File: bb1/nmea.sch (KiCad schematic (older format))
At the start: 30 parts, among them P1 PWR+CAN, P5 NMEA_RX, P7 NMEA_TX, P8 BATTERIES, P9 SHUNT, U10 MCP2562, U11 SN75C3222E, U12 INA219

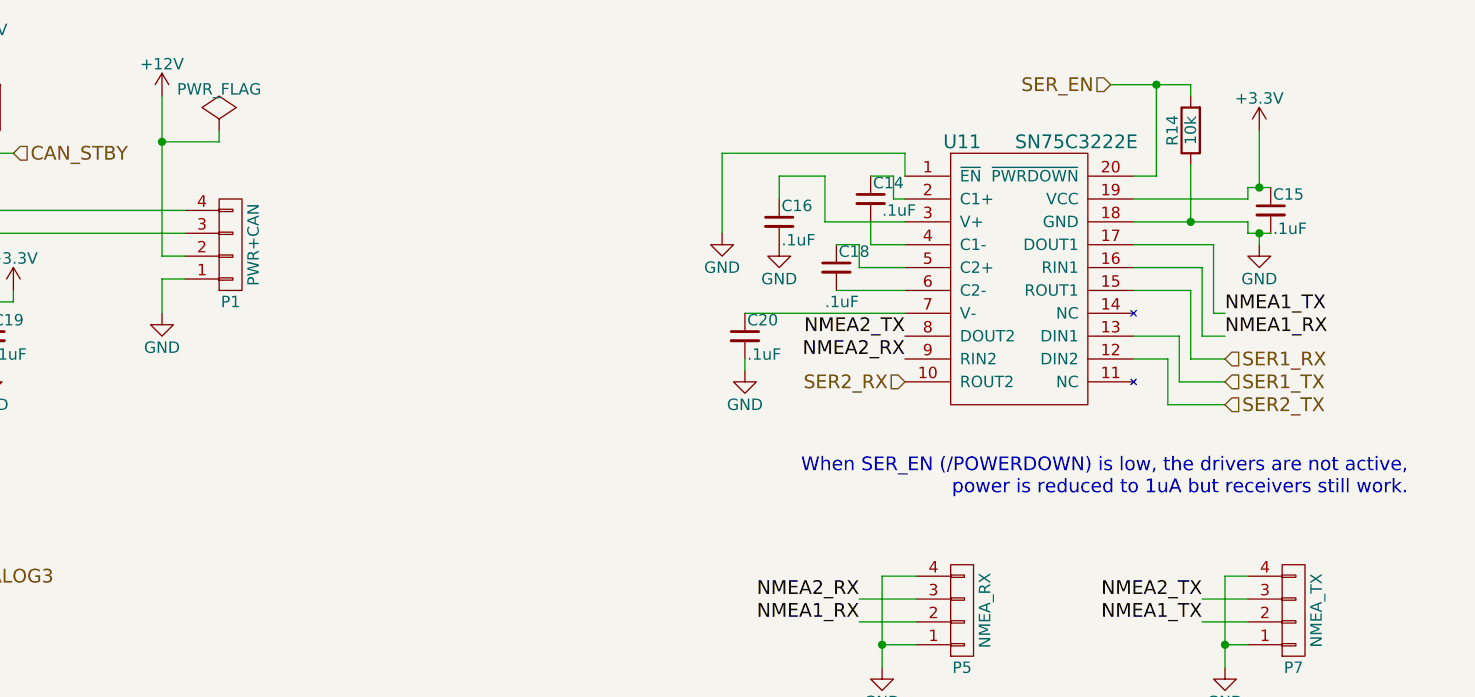
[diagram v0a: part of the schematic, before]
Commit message: Fine tuning of the board
- Added test headers for serial1, serial2 and can (at 3.3v levels)
- Added solder jumpers to disconnect serial2 from rs232 converter
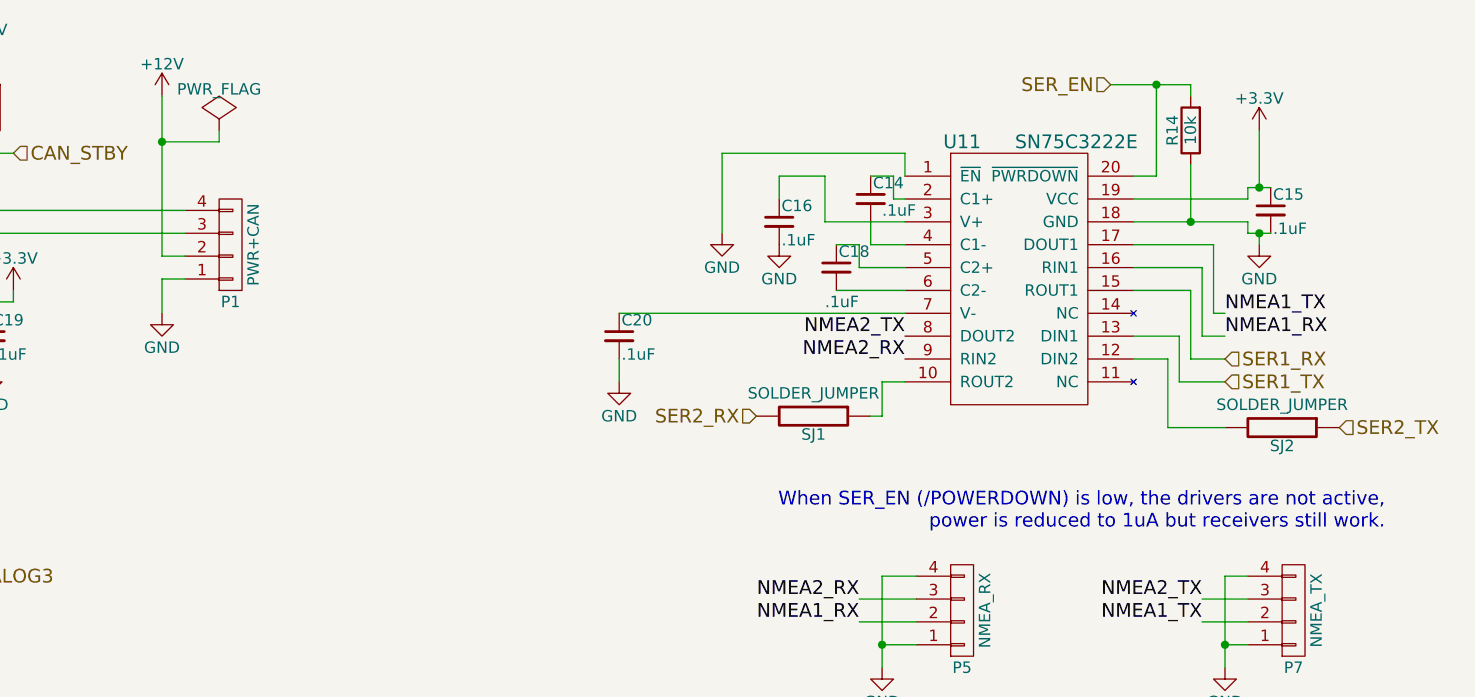
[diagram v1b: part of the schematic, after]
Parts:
- added SJ1, SJ2: SOLDER_JUMPER, bb:SolderJumper, symbol SOLDER_JUMPER
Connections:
- net SER2_RX: now also SJ1.2; no longer U11.10 (ROUT2)
- net SER2_TX: now also SJ2.1; no longer U11.12 (DIN2)
- new net: SJ1.1, U11.10 (ROUT2)
- new net: SJ2.2, U11.12 (DIN2)
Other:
- moved on the sheet: C20
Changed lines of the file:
@@
 L C_Small C20
 U 1 1 56606B8F
-P 6700 2400
-F 0 "C20" H 6710 2470 50  0000 L CNN
-F 1 ".1uF" H 6710 2320 50  0000 L CNN
-F 2 "Capacitors_SMD:C_0603_HandSoldering" H 6700 2400 60  0001 C CNN
-F 3 "" H 6700 2400 60  0000 C CNN
-	1    6700 2400
+P 6150 2400
+F 0 "C20" H 6160 2470 50  0000 L CNN
+F 1 ".1uF" H 6160 2320 50  0000 L CNN
+F 2 "Capacitors_SMD:C_0603_HandSoldering" H 6150 2400 60  0001 C CNN
+F 3 "" H 6150 2400 60  0000 C CNN
+	1    6150 2400
 	1    0    0    -1
 $EndComp
@@
 	7100 2200 7400 2200
 Wire Wire Line
-	7400 2300 6700 2300
-Wire Wire Line
-	6700 2500 6700 2550
+	7400 2300 6150 2300
+Wire Wire Line
+	6150 2500 6150 2600
 $Comp
 L GND #PWR064
 U 1 1 56606BD2
-P 6700 2550
-F 0 "#PWR064" H 6700 2300 50  0001 C CNN
-F 1 "GND" H 6700 2400 50  0000 C CNN
-F 2 "" H 6700 2550 60  0000 C CNN
-F 3 "" H 6700 2550 60  0000 C CNN
-	1    6700 2550
+P 6150 2600
+F 0 "#PWR064" H 6150 2350 50  0001 C CNN
+F 1 "GND" H 6150 2450 50  0000 C CNN
+F 2 "" H 6150 2600 60  0000 C CNN
+F 3 "" H 6150 2600 60  0000 C CNN
+	1    6150 2600
 	1    0    0    -1
 $EndComp
@@
 	8400 2500 8550 2500
 Wire Wire Line
-	8550 2500 8550 2700
-Wire Wire Line
-	8550 2700 8800 2700
+	8550 2500 8550 2800
+Wire Wire Line
+	8550 2800 8800 2800
 Text Label 7400 2400 2    60   ~ 0
 NMEA2_TX
@@
 Text HLabel 2350 1750 0    60   Input ~ 0
 CAN_TX
-Text HLabel 7400 2600 0    60   Input ~ 0
+Text HLabel 6750 2750 0    60   Input ~ 0
 SER2_RX
 Text HLabel 8800 2500 2    60   Input ~ 0
@@
 Text HLabel 8800 2600 2    60   Input ~ 0
 SER1_TX
-Text HLabel 8800 2700 2    60   Input ~ 0
+Text HLabel 9300 2800 2    60   Input ~ 0
 SER2_TX
 Text HLabel 3200 4650 2    60   Input ~ 0
@@
 Text HLabel 8300 1300 0    60   Input ~ 0
 SER_EN
-Text Notes 9600 3100 2    60   ~ 0
+Text Notes 9500 3250 2    60   ~ 0
 When SER_EN (/POWERDOWN) is low, the drivers are not active, \npower is reduced to 1uA but receivers still work.
 $Comp
@@
 $EndComp
 Wire Wire Line
-	4250 2050 4150 2050
-Wire Wire Line
-	4150 2050 4150 1350
+	4150 2050 4250 2050
+Wire Wire Line
+	4150 1350 4150 2050
 Wire Wire Line
 	4250 2150 4150 2150
@@
 	2050 6150 1850 6150
 Connection ~ 1850 6150
+Wire Wire Line
+	7400 2600 7300 2600
+Wire Wire Line
+	7300 2600 7300 2750
+Wire Wire Line
+	7300 2750 7250 2750
+$Comp
+L SOLDER_JUMPER SJ1
+U 1 1 566032C9
+P 7000 2750
+F 0 "SJ1" V 7080 2750 50  0000 C CNN
+F 1 "SOLDER_JUMPER" V 6900 2750 50  0000 C CNN
+F 2 "bb:SolderJumper" H 7000 2750 60  0001 C CNN
+F 3 "" H 7000 2750 60  0000 C CNN
+	1    7000 2750
+	0    1    1    0
+$EndComp
+$Comp
+L SOLDER_JUMPER SJ2
+U 1 1 56603397
+P 9050 2800
+F 0 "SJ2" V 9130 2800 50  0000 C CNN
+F 1 "SOLDER_JUMPER" V 8950 2800 50  0000 C CNN
+F 2 "bb:SolderJumper" H 9050 2800 60  0001 C CNN
+F 3 "" H 9050 2800 60  0000 C CNN
+	1    9050 2800
+	0    1    1    0
+$EndComp
 $EndSCHEMATC

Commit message: Continued work on the PCB. Lots of footprint work.
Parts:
- U10: footprint SMD_Packages:SOIC-8-N -> gsg-modules:SOIC8-208
- U11: footprint SMD_Packages:SSOP-20 -> bb:SSOP-20-HandSoldering
- U12: footprint bb:INA219 -> gsg-modules:SOIC8-208
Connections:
- net SER2_RX: now also SJ1.1, U11.10 (ROUT2)
- net SER2_TX: now also SJ2.2, U11.12 (DIN2)

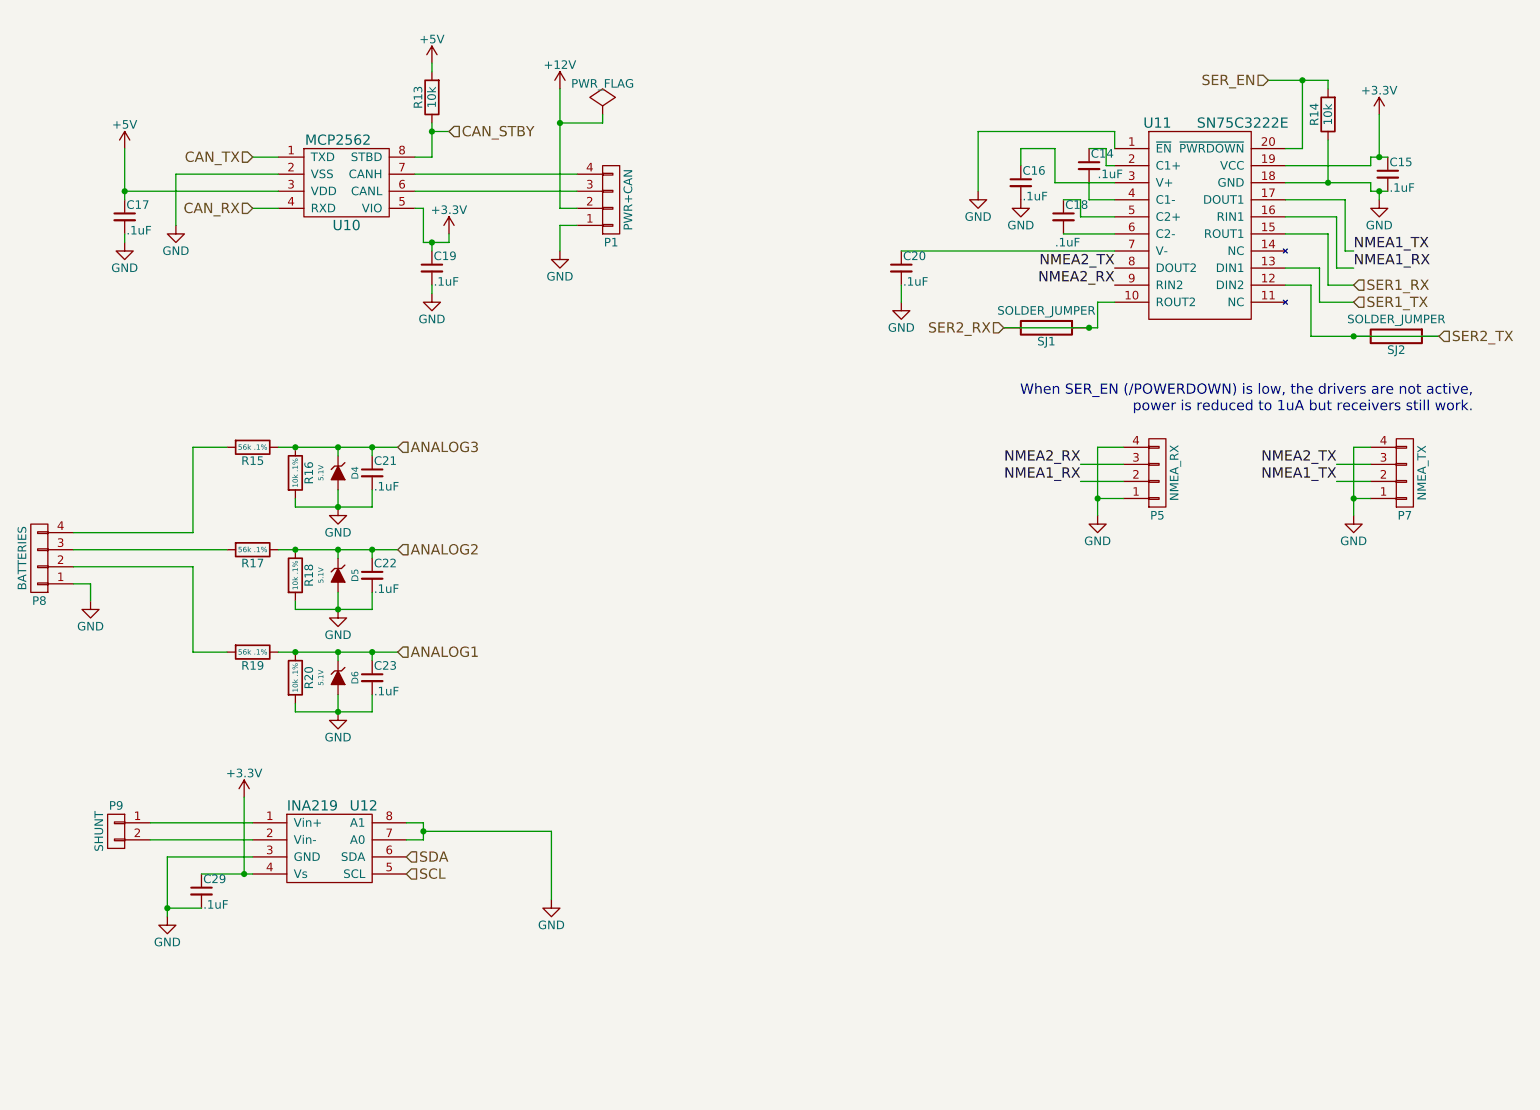
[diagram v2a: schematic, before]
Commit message: Finalized v1 revA
 - Added BNO055
 - Fixed SOIC8 pattern
 - Replaced phoenix connectors by a 20 pol
 - Many fine tuning/cosmetic adjustments
 - Sent files to manufacturing. Will tag this commit.
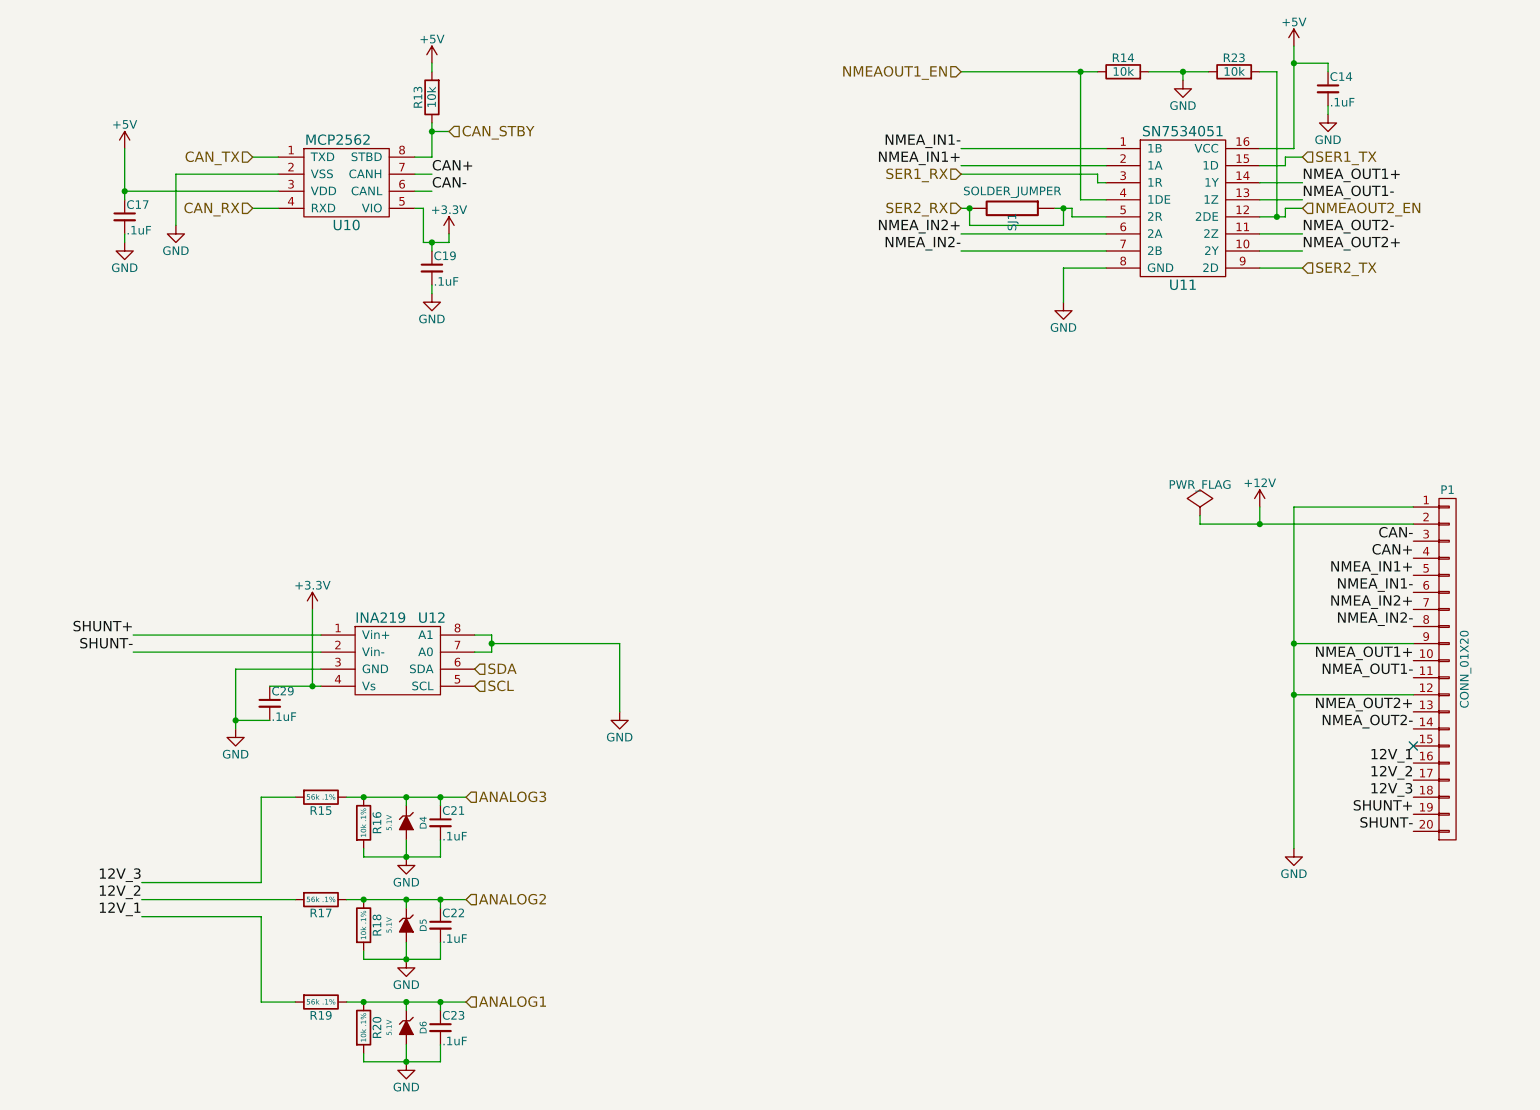
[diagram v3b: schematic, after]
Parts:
- removed C15, C16, C18, C20: .1uF, Capacitors_SMD:C_0603_HandSoldering, symbol C_Small
- removed P1: PWR+CAN, Terminal_Blocks:TerminalBlock_Pheonix_PT-3.5mm_4pol, symbol CONN_01X04
- removed P5: NMEA_RX, Terminal_Blocks:TerminalBlock_Pheonix_PT-3.5mm_4pol, symbol CONN_01X04
- removed P7: NMEA_TX, Terminal_Blocks:TerminalBlock_Pheonix_PT-3.5mm_4pol, symbol CONN_01X04
- removed P8: BATTERIES, Terminal_Blocks:TerminalBlock_Pheonix_PT-3.5mm_4pol, symbol CONN_01X04
- removed P9: SHUNT, Terminal_Blocks:TerminalBlock_Pheonix_PT-3.5mm_2pol, symbol CONN_01X02
- removed SJ1: SOLDER_JUMPER, bb:SolderJumper, symbol SOLDER_JUMPER
- removed U11: SN75C3222E, bb:SSOP-20-HandSoldering, symbol SN75C3222E
- added P1: CONN_01X20, bb:TerminalBlock_Pheonix_PT-3.5mm_20pol, symbol CONN_01X20
- added R23: 10k, Resistors_SMD:R_0603_HandSoldering, symbol R
- added U11: SN7534051, bb:SOIC-16_5.6x10.5mm_Pitch1.27mm-HandSolder, symbol SN7534051
- U10, U12: footprint gsg-modules:SOIC8-208 -> bb:SOIC8N-HandSoldering
- renumbered SJ2 to SJ1
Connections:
- net SER_EN is gone; now on net GND: R14.2
- net +12V: now also P1.2 (P2)
- net +5V: now also C14.1, U11.16 (VCC)
- net GND: now also C14.2, P1.1 (P1), P1.12 (P12), P1.9 (P9), R23.1, U11.8 (GND); no longer R14.1
- net SER1_RX: now also U11.3 (1R)
- net SER1_TX: now also U11.15 (1D)
- net SER2_RX: now also SJ1.1, SJ1.2, U11.5 (2R)
- net SER2_TX: now also U11.9 (2D); no longer SJ1.1, SJ1.2
- net 12V_3: now reaches R15.2
- net 12V_3: now also P1.18 (P18)
- net CAN-: now reaches U10.6 (CANL)
- net CAN-: now also P1.3 (P3)
- net CAN+: now reaches U10.7 (CANH)
- net CAN+: now also P1.4 (P4)
- net SHUNT+: now reaches U12.1 (Vin+)
- net SHUNT+: now also P1.19 (P19)
- net SHUNT-: now reaches U12.2 (Vin-)
- net SHUNT-: now also P1.20 (P20)
- net 12V_2: now reaches R17.2
- net 12V_2: now also P1.17 (P17)
- net 12V_1: now reaches R19.2
- net 12V_1: now also P1.16 (P16)
- new net NMEAOUT1_EN: R14.1, U11.4 (1DE)
- new net NMEAOUT2_EN: R23.2, U11.12 (2DE)
- new net NMEA_IN1+: P1.5 (P5), U11.2 (1A)
- new net NMEA_IN1-: P1.6 (P6), U11.1 (1B)
- new net NMEA_IN2+: P1.7 (P7), U11.6 (2A)
- new net NMEA_IN2-: P1.8 (P8), U11.7 (2B)
- new net NMEA_OUT1+: P1.10 (P10), U11.14 (1Y)
- new net NMEA_OUT1-: P1.11 (P11), U11.13 (1Z)
- new net NMEA_OUT2+: P1.13 (P13), U11.10 (2Y)
- new net NMEA_OUT2-: P1.14 (P14), U11.11 (2Z)
- no-connect marks 0 -> 1
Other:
- note removed: "When SER_EN (/POWERDOWN) is low, the drivers are not active, \npower is reduced to 1uA but receivers still work."
- moved on the sheet: C21, C22, C23, C29, D4, D5, D6, R15, R16, R17, R18, R19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
